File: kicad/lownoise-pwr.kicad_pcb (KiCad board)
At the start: 2 copper layers, 78 x 36.9 mm, 26 parts, among them J1 Conn_01x02_Female, J2 Conn_01x02_Female, J3 Conn_01x02_Female, Q1 BD244C / MJD6284, U1 LM723_DIP14, U2 LM4040DBZ-4.1

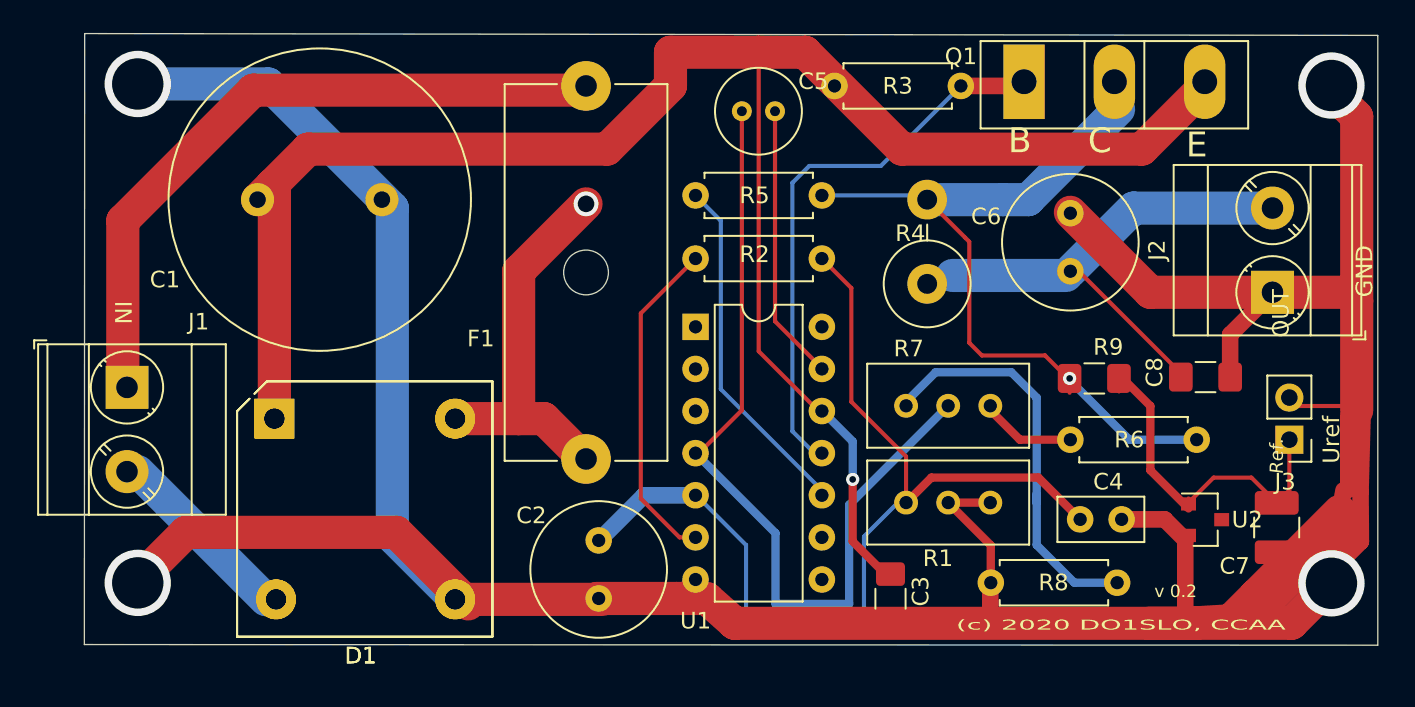
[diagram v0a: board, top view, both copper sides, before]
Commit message: Ensure distance to pcb-edge, places C4, C9
New component requires redesign
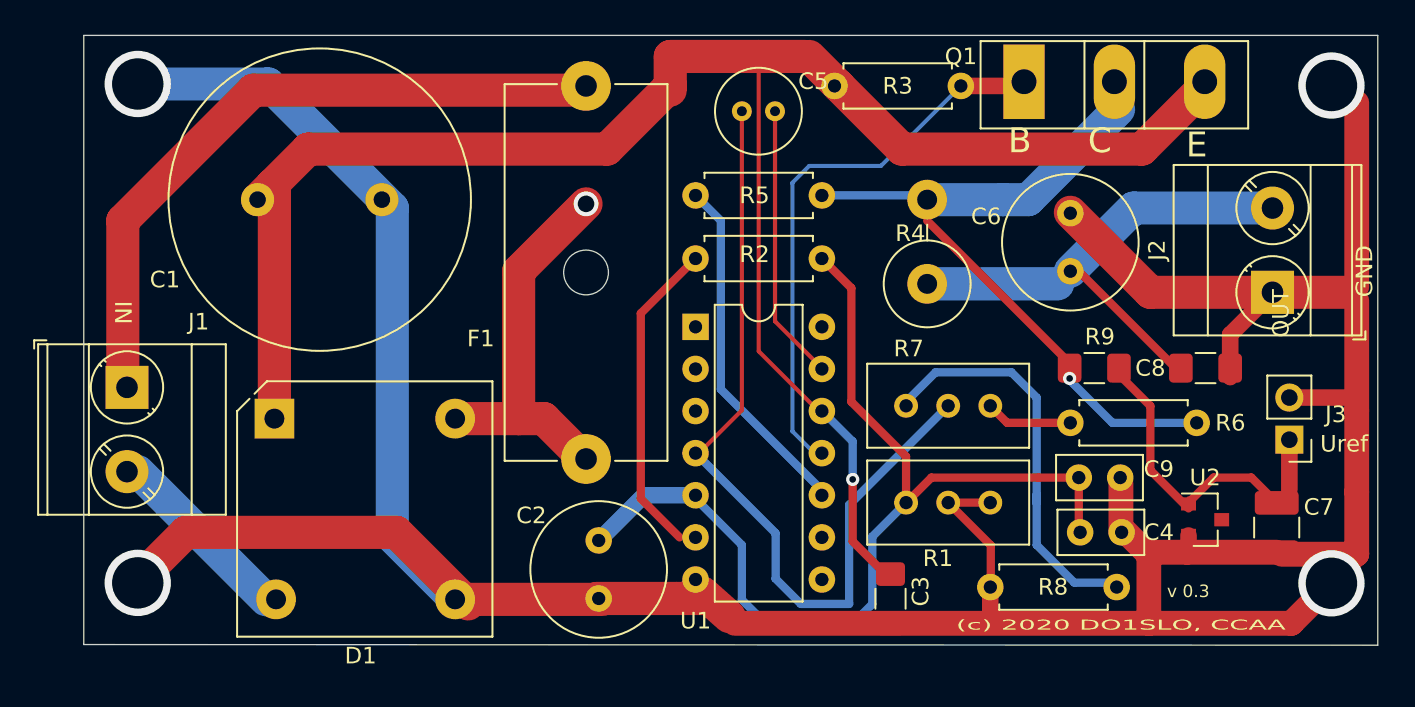
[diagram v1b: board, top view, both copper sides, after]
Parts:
- removed the D1 at (57.1, 83.1)
- added C9: 500n, Capacitor_THT:C_Disc_D5.0mm_W2.5mm_P2.50mm, F.Cu at (105.6, 86.6)
- C4: value 1000n -> 500n
- moved R6 1.02 mm to (112.7, 83.3)
- moved C4 0.78 mm to (105.7, 89.9)
- moved R9 0.62 mm to (106.5, 80.0)
- moved C8 0.54 mm to (113.3, 80.0)
- moved R8 0.27 mm to (107.9, 93.2)
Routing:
- net GND: track 239.7 -> 218.5 mm
- net Net-(Q1-Pad2): track 47.2 -> 42.7 mm
- net Net-(C2-Pad1): track 60.7 -> 62.9 mm
- net Net-(C6-Pad1): track 30.6 -> 32.7 mm
- net Net-(C5-Pad1): track 53.3 -> 52.4 mm
- net Net-(C7-Pad1): track 22.0 -> 21.3 mm
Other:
- board size 78 x 36.9 mm -> 78 x 36.8 mm
- board text added: "v 0.3"
- board text removed: "DO1SLO"
- board text removed: "Ref."
- board text removed: "v 0.2"
